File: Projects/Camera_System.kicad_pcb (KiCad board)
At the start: 2 copper layers, 10 parts, among them J1 BARREL_JACK, U1 IFX1117ME_V33, U2 LD2980ABM50TR

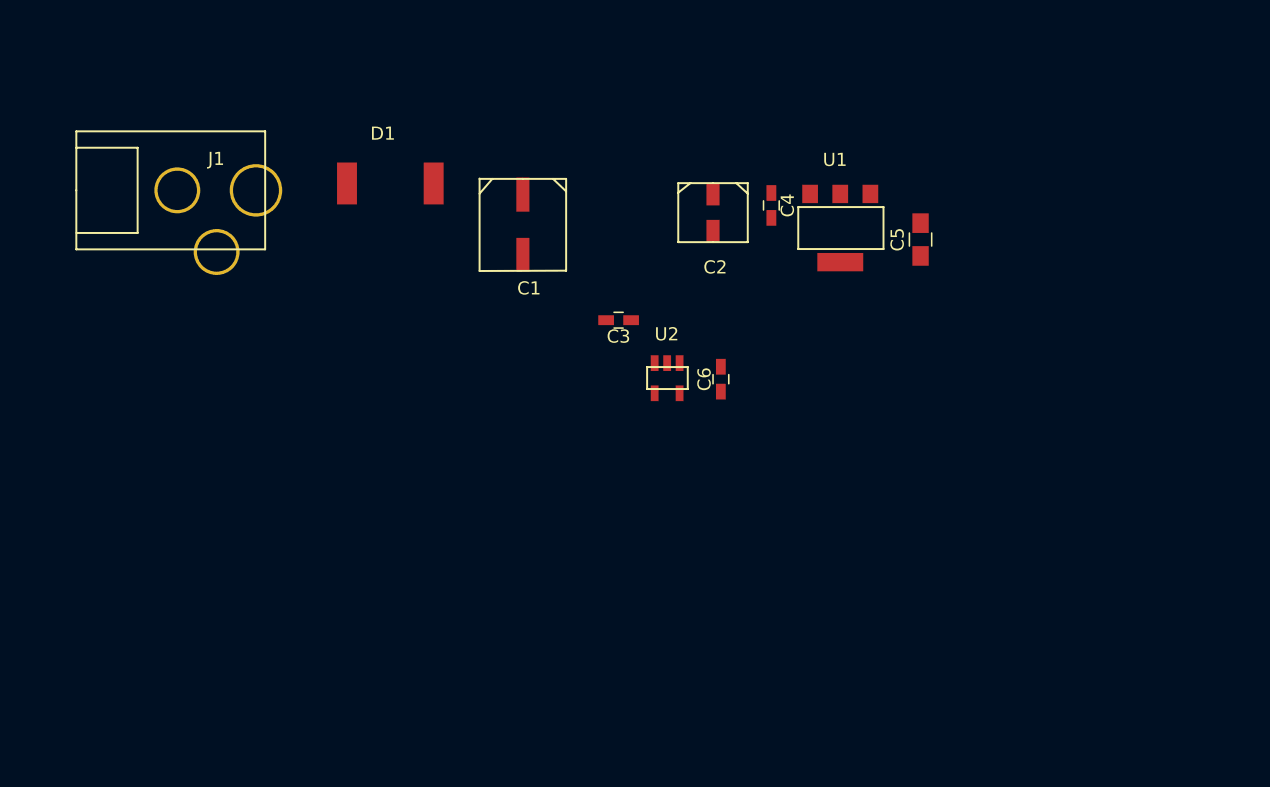
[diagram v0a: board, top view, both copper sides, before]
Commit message: New symbols habe been added
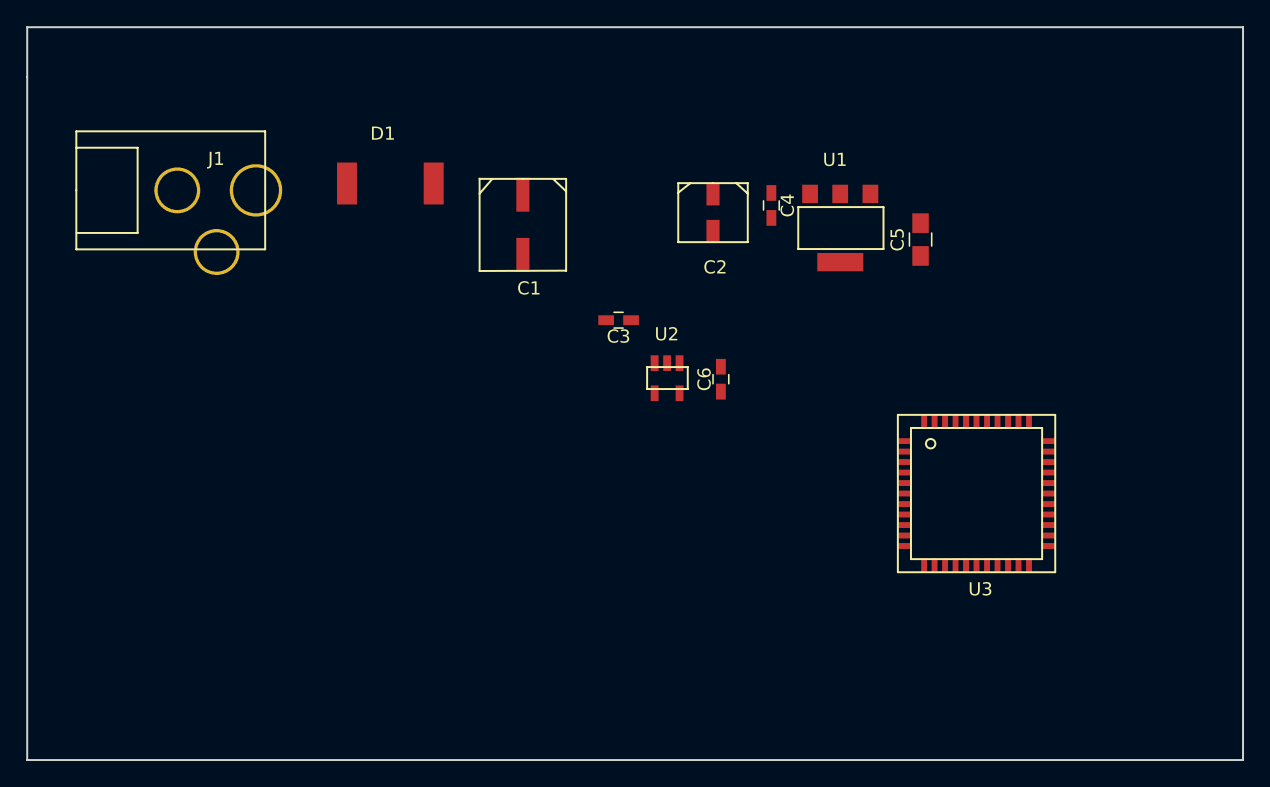
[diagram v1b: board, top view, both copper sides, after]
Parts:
- added U3: ATMEGA16A-AU, MyLibraries:ATMEGA16A-AU, F.Cu at (172.7, 121.9)
- C5: value 22u -> ???
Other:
- board outline added: 92.7 x 55.9 mm
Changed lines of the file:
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@@
 (kicad_pcb (version 4) (host pcbnew 4.0.6)
   (general
-    (links 20)
-    (no_connects 20)
+    (links 27)
+    (no_connects 27)
     (area 0 0 0 0)
     (thickness 1.6)
-    (drawings 0)
+    (drawings 5)
     (tracks 0)
     (zones 0)
-    (modules 10)
+    (modules 11)
     (nets 6)
   )
@@
       (effects (font (size 1 1) (thickness 0.15)))
     )
-    (fp_text value 22u (at 0 1.75 90) (layer F.Fab)
+    (fp_text value ??? (at 0 1.75 90) (layer F.Fab)
       (effects (font (size 1 1) (thickness 0.15)))
     )
@@
     (pad 4 smd rect (at 0.95 -2.3 180) (size 0.6 1.2) (layers F.Cu F.Paste F.Mask))
   )
+  (module MyLibraries:ATMEGA16A-AU (layer F.Cu)
+    (at 172.72 121.92)
+    (fp_text reference U3 (at 0.3 7.3) (layer F.SilkS)
+      (effects (font (size 1 1) (thickness 0.15)))
+    )
+    (fp_text value ATMEGA16A-AU (at 0.5 -7) (layer F.Fab)
+      (effects (font (size 1 1) (thickness 0.15)))
+    )
+    (fp_line (start -5 -5) (end 5 -5) (layer F.SilkS) (width 0.15))
+    (fp_line (start 5 -5) (end 5 5) (layer F.SilkS) (width 0.15))
+    (fp_line (start 5 5) (end -5 5) (layer F.SilkS) (width 0.15))
+    (fp_line (start -5 5) (end -5 -5) (layer F.SilkS) (width 0.15))
+    (fp_circle (center -3.5 -3.8) (end -3.2 -3.6) (layer F.SilkS) (width 0.15))
+    (fp_line (start -6 6) (end -6 -6) (layer F.SilkS) (width 0.15))
+    (fp_line (start -6 -6) (end 6 -6) (layer F.SilkS) (width 0.15))
+    (fp_line (start 6 -6) (end 6 6) (layer F.SilkS) (width 0.15))
+    (fp_line (start 6 6) (end -6 6) (layer F.SilkS) (width 0.15))
+    (pad 28 smd rect (at 5.5 0) (size 1.1 0.45) (layers F.Cu F.Paste F.Mask)
+      (net 1 GND))
+    (pad 29 smd rect (at 5.5 -0.8) (size 1.1 0.45) (layers F.Cu F.Paste F.Mask))
+    (pad 30 smd rect (at 5.5 -1.6) (size 1.1 0.45) (layers F.Cu F.Paste F.Mask))
+    (pad 31 smd rect (at 5.5 -2.4) (size 1.1 0.45) (layers F.Cu F.Paste F.Mask))
+    (pad 32 smd rect (at 5.5 -3.2) (size 1.1 0.45) (layers F.Cu F.Paste F.Mask))
+    (pad 33 smd rect (at 5.5 -4) (size 1.1 0.45) (layers F.Cu F.Paste F.Mask))
+    (pad 27 smd rect (at 5.5 0.8) (size 1.1 0.45) (layers F.Cu F.Paste F.Mask))
+    (pad 26 smd rect (at 5.5 1.6) (size 1.1 0.45) (layers F.Cu F.Paste F.Mask))
+    (pad 25 smd rect (at 5.5 2.4) (size 1.1 0.45) (layers F.Cu F.Paste F.Mask))
+    (pad 24 smd rect (at 5.5 3.2) (size 1.1 0.45) (layers F.Cu F.Paste F.Mask))
+    (pad 23 smd rect (at 5.5 4) (size 1.1 0.45) (layers F.Cu F.Paste F.Mask))
+    (pad 17 smd rect (at 0 5.5) (size 0.45 1.1) (layers F.Cu F.Paste F.Mask)
+      (net 2 +3V3))
+    (pad 18 smd rect (at 0.8 5.5) (size 0.45 1.1) (layers F.Cu F.Paste F.Mask)
+      (net 1 GND))
+    (pad 19 smd rect (at 1.6 5.5) (size 0.45 1.1) (layers F.Cu F.Paste F.Mask))
+    (pad 20 smd rect (at 2.4 5.5) (size 0.45 1.1) (layers F.Cu F.Paste F.Mask))
+    (pad 21 smd rect (at 3.2 5.5) (size 0.45 1.1) (layers F.Cu F.Paste F.Mask))
+    (pad 22 smd rect (at 4 5.5) (size 0.45 1.1) (layers F.Cu F.Paste F.Mask))
+    (pad 16 smd rect (at -0.8 5.5) (size 0.45 1.1) (layers F.Cu F.Paste F.Mask))
+    (pad 15 smd rect (at -1.6 5.5) (size 0.45 1.1) (layers F.Cu F.Paste F.Mask))
+    (pad 14 smd rect (at -2.4 5.5) (size 0.45 1.1) (layers F.Cu F.Paste F.Mask))
+    (pad 13 smd rect (at -3.2 5.5) (size 0.45 1.1) (layers F.Cu F.Paste F.Mask))
+    (pad 12 smd rect (at -4 5.5) (size 0.45 1.1) (layers F.Cu F.Paste F.Mask))
+    (pad 39 smd rect (at 0 -5.5) (size 0.45 1.1) (layers F.Cu F.Paste F.Mask)
+      (net 1 GND))
+    (pad 38 smd rect (at 0.8 -5.5) (size 0.45 1.1) (layers F.Cu F.Paste F.Mask)
+      (net 2 +3V3))
+    (pad 37 smd rect (at 1.6 -5.5) (size 0.45 1.1) (layers F.Cu F.Paste F.Mask))
+    (pad 36 smd rect (at 2.4 -5.5) (size 0.45 1.1) (layers F.Cu F.Paste F.Mask))
+    (pad 35 smd rect (at 3.2 -5.5) (size 0.45 1.1) (layers F.Cu F.Paste F.Mask))
+    (pad 34 smd rect (at 4 -5.5) (size 0.45 1.1) (layers F.Cu F.Paste F.Mask))
+    (pad 40 smd rect (at -0.8 -5.5) (size 0.45 1.1) (layers F.Cu F.Paste F.Mask))
+    (pad 41 smd rect (at -1.6 -5.5) (size 0.45 1.1) (layers F.Cu F.Paste F.Mask))
+    (pad 42 smd rect (at -2.4 -5.5) (size 0.45 1.1) (layers F.Cu F.Paste F.Mask))
+    (pad 43 smd rect (at -3.2 -5.5) (size 0.45 1.1) (layers F.Cu F.Paste F.Mask))
+    (pad 44 smd rect (at -4 -5.5) (size 0.45 1.1) (layers F.Cu F.Paste F.Mask))
+    (pad 6 smd rect (at -5.5 0) (size 1.1 0.45) (layers F.Cu F.Paste F.Mask)
+      (net 1 GND))
+    (pad 5 smd rect (at -5.5 -0.8) (size 1.1 0.45) (layers F.Cu F.Paste F.Mask)
+      (net 2 +3V3))
+    (pad 4 smd rect (at -5.5 -1.6) (size 1.1 0.45) (layers F.Cu F.Paste F.Mask))
+    (pad 3 smd rect (at -5.5 -2.4) (size 1.1 0.45) (layers F.Cu F.Paste F.Mask))
+    (pad 2 smd rect (at -5.5 -3.2) (size 1.1 0.45) (layers F.Cu F.Paste F.Mask))
+    (pad 1 smd rect (at -5.5 -4) (size 1.1 0.45) (layers F.Cu F.Paste F.Mask))
+    (pad 7 smd rect (at -5.5 0.8) (size 1.1 0.45) (layers F.Cu F.Paste F.Mask))
+    (pad 8 smd rect (at -5.5 1.6) (size 1.1 0.45) (layers F.Cu F.Paste F.Mask))
+    (pad 9 smd rect (at -5.5 2.4) (size 1.1 0.45) (layers F.Cu F.Paste F.Mask))
+    (pad 10 smd rect (at -5.5 3.2) (size 1.1 0.45) (layers F.Cu F.Paste F.Mask))
+    (pad 11 smd rect (at -5.5 4) (size 1.1 0.45) (layers F.Cu F.Paste F.Mask))
+  )
+  (gr_line (start 100.33 86.36) (end 100.33 90.17) (angle 90) (layer Edge.Cuts) (width 0.15))
+  (gr_line (start 193.04 86.36) (end 100.33 86.36) (angle 90) (layer Edge.Cuts) (width 0.15))
+  (gr_line (start 193.04 142.24) (end 193.04 86.36) (angle 90) (layer Edge.Cuts) (width 0.15))
+  (gr_line (start 100.33 142.24) (end 193.04 142.24) (angle 90) (layer Edge.Cuts) (width 0.15))
+  (gr_line (start 100.33 90.17) (end 100.33 142.24) (angle 90) (layer Edge.Cuts) (width 0.15))
 )

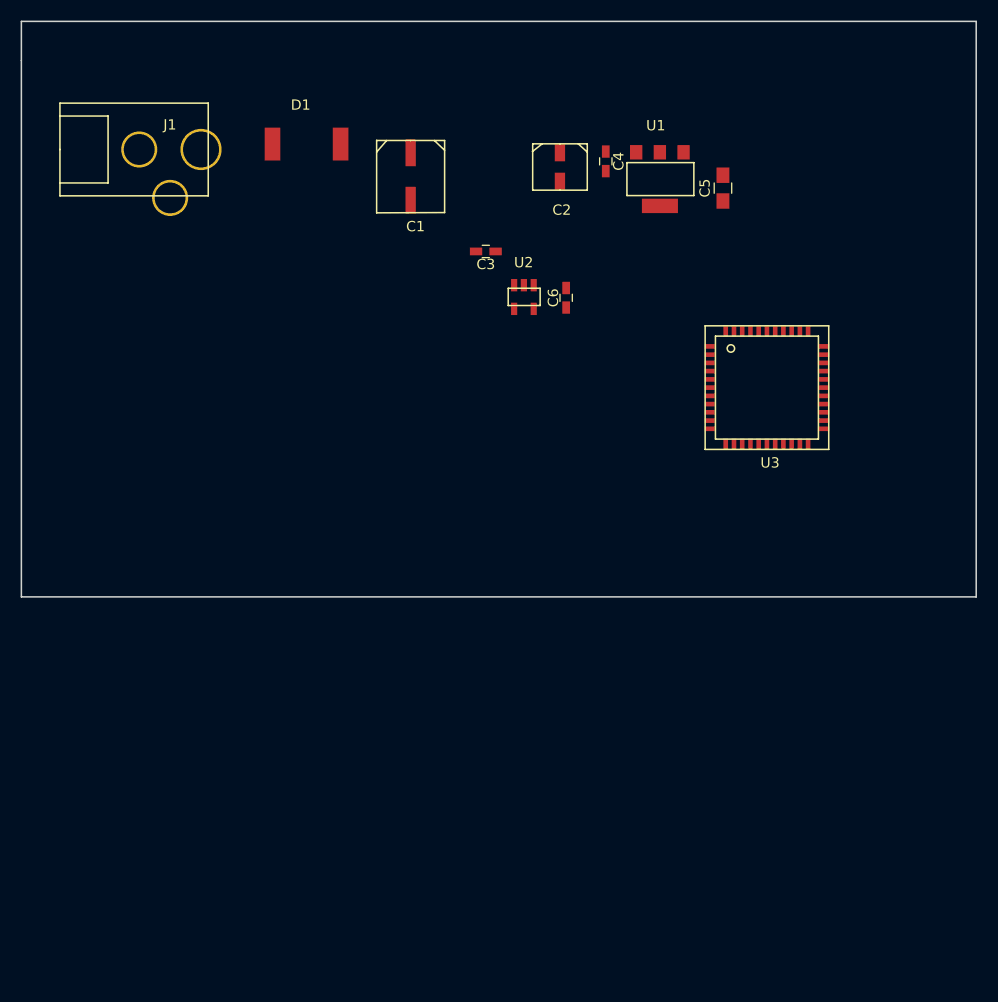
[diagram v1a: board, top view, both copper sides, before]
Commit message: New footprints have been created
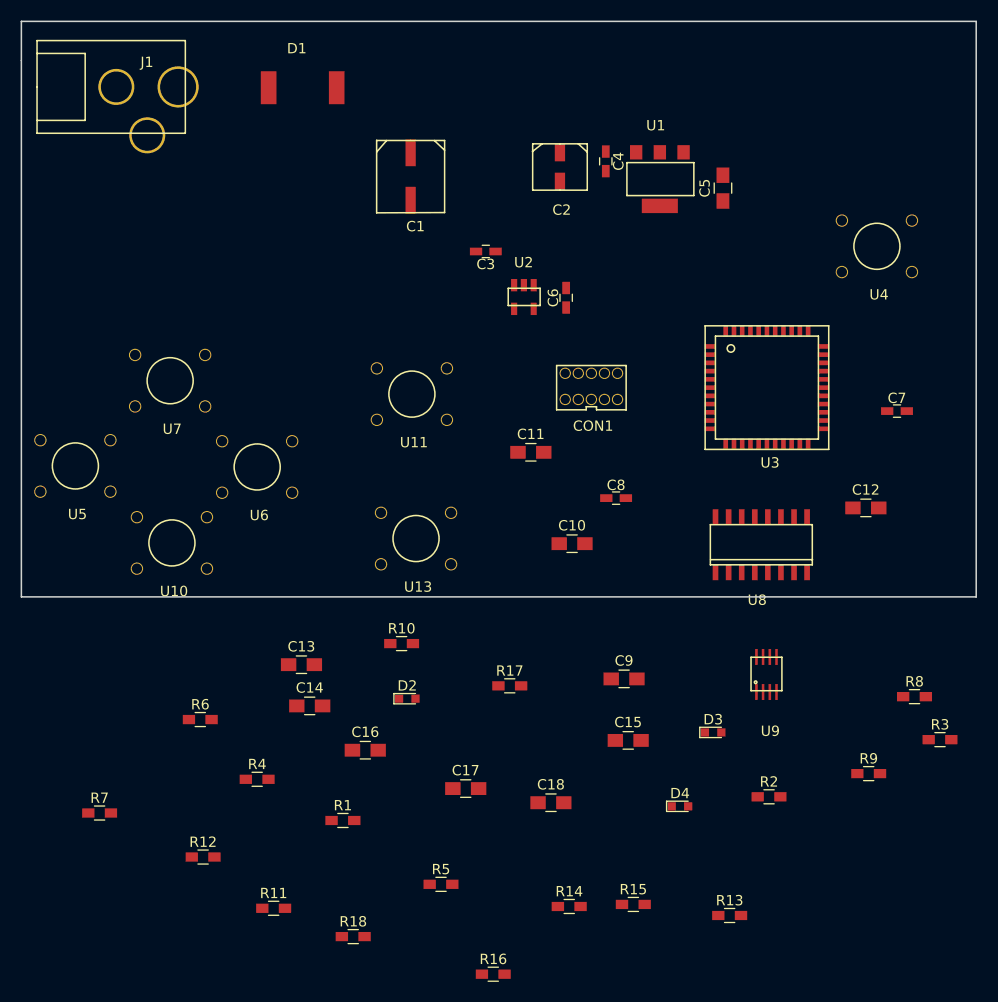
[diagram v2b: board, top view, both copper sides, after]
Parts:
- added C10: 100n, Capacitors_SMD:C_0805_HandSoldering, F.Cu at (153.8, 137.1)
- added C11: 100n, Capacitors_SMD:C_0805_HandSoldering, F.Cu at (149.8, 128.2)
- added C12: 100n, Capacitors_SMD:C_0805_HandSoldering, F.Cu at (182.3, 133.6)
- added C13: 100n, Capacitors_SMD:C_0805_HandSoldering, F.Cu at (127.5, 148.8)
- added C14: 100n, Capacitors_SMD:C_0805_HandSoldering, F.Cu at (128.3, 152.8)
- added C15: 100n, Capacitors_SMD:C_0805_HandSoldering, F.Cu at (159.2, 156.2)
- added C16: 100n, Capacitors_SMD:C_0805_HandSoldering, F.Cu at (133.7, 157.1)
- added C17: 100n, Capacitors_SMD:C_0805_HandSoldering, F.Cu at (143.5, 160.8)
- added C18: 100n, Capacitors_SMD:C_0805_HandSoldering, F.Cu at (151.8, 162.2)
- added C7: 12p, Capacitors_SMD:C_0603_HandSoldering, F.Cu at (185.3, 124.2)
- added C8: 12p, Capacitors_SMD:C_0603_HandSoldering, F.Cu at (158.1, 132.7)
- added C9: 100n, Capacitors_SMD:C_0805_HandSoldering, F.Cu at (158.8, 150.2)
- added CON1: AVR-ISP-10, MyLibraries:N2510-6002RB, F.Cu at (155.7, 121.8)
- added D2: LED, LEDs:LED_0603, F.Cu at (137.8, 152.1)
- added D3: LED, LEDs:LED_0603, F.Cu at (167.5, 155.4)
- added D4: LED, LEDs:LED_0603, F.Cu at (164.3, 162.6)
- added R1: 0, Resistors_SMD:R_0603_HandSoldering, F.Cu at (131.6, 163.9)
- added R10: 1.74k, Resistors_SMD:R_0603_HandSoldering, F.Cu at (137.2, 146.8)
- added R11: 10k, Resistors_SMD:R_0603_HandSoldering, F.Cu at (124.8, 172.5)
- added R12: 10k, Resistors_SMD:R_0603_HandSoldering, F.Cu at (118.0, 167.5)
- added R13: 200k, Resistors_SMD:R_0603_HandSoldering, F.Cu at (169.1, 173.2)
- added R14: 10k, Resistors_SMD:R_0603_HandSoldering, F.Cu at (153.5, 172.3)
- added R15: 10k, Resistors_SMD:R_0603_HandSoldering, F.Cu at (159.8, 172.1)
- added R16: 4.7k, Resistors_SMD:R_0603_HandSoldering, F.Cu at (146.2, 178.9)
- added R17: 24.9, Resistors_SMD:R_0603_HandSoldering, F.Cu at (147.8, 150.9)
- added R18: 4.7k, Resistors_SMD:R_0603_HandSoldering, F.Cu at (132.6, 175.2)
- added R2: 620, Resistors_SMD:R_0603_HandSoldering, F.Cu at (172.9, 161.7)
- added R3: 10k, Resistors_SMD:R_0603_HandSoldering, F.Cu at (189.5, 156.1)
- added R4: 620, Resistors_SMD:R_0603_HandSoldering, F.Cu at (123.2, 159.9)
- added R5: 1k, Resistors_SMD:R_0603_HandSoldering, F.Cu at (141.1, 170.2)
- added R6: 10k, Resistors_SMD:R_0603_HandSoldering, F.Cu at (117.7, 154.2)
- added R7: 10k, Resistors_SMD:R_0603_HandSoldering, F.Cu at (107.9, 163.2)
- added R8: 10k, Resistors_SMD:R_0603_HandSoldering, F.Cu at (187.1, 151.9)
- added R9: 1.74k, Resistors_SMD:R_0603_HandSoldering, F.Cu at (182.6, 159.4)
- added U10: RT1105AF160Q, MyLibraries:RT1105AF160Q, F.Cu at (115.0, 137.0)
- added U11: RT1105AF160Q, MyLibraries:RT1105AF160Q, F.Cu at (138.2, 122.5)
- added U13: RT1105AF160Q, MyLibraries:RT1105AF160Q, F.Cu at (138.7, 136.6)
- added U4: RT1105AF160Q, MyLibraries:RT1105AF160Q, F.Cu at (183.4, 108.2)
- added U5: RT1105AF160Q, MyLibraries:RT1105AF160Q, F.Cu at (105.6, 129.5)
- added U6: RT1105AF160Q, MyLibraries:RT1105AF160Q, F.Cu at (123.2, 129.6)
- added U7: RT1105AF160Q, MyLibraries:RT1105AF160Q, F.Cu at (114.8, 121.2)
- added U8: CD4014B, MyLibraries:CD4014B_SOIC, F.Cu at (172.2, 137.2)
- added U9: PCA9306, MyLibraries:PCA9306_SM8, F.Cu at (172.7, 149.8)
- C5: value ??? -> 22u
- moved J1 6.47 mm to (112.5, 92.7)
- moved D1 5.49 mm to (130.9, 92.8)
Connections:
- U3 pad 1: (no net) -> /MOSI
- U3 pad 14: (no net) -> /P_S_CLK
- U3 pad 19: (no net) -> /3V3_SCL
- U3 pad 2: (no net) -> /MISO
- U3 pad 20: (no net) -> /3V3_SDA
- U3 pad 27: (no net) -> +3V3
- U3 pad 29: (no net) -> Net-(C9-Pad1)
- U3 pad 3: (no net) -> /SCK
- U3 pad 4: (no net) -> /MIC_RST
- U3 pad 40: (no net) -> /SERIAL_IN
- U3 pad 41: (no net) -> /P_S_CTRL
- U3 pad 43: (no net) -> Net-(R1-Pad2)
- U3 pad 7: (no net) -> Net-(C7-Pad1)
- U3 pad 8: (no net) -> Net-(C8-Pad1)

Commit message: Schematic has been finished and layout started
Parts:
- added U12: LCD_1602, MyLibraries:LCD_header_2.5_4, F.Cu at (158.9, 43.6)
- added U14: Si501, MyLibraries:Si501_2x2.5, F.Cu at (233.6, 152.7)
- added U15: OV7670-nofifo, MyLibraries:Camera_ov7670_2.5_2x9, F.Cu at (106.6, 152.7)
- added U16: ESP8266, MyLibraries:wifi_header_female_2.5_2x4, F.Cu at (91.9, 79.8)
- added U17: SDCARD, MyLibraries:SDCARD_2.5_6, F.Cu at (70.2, 98.3)
- added Y1: Crystal, MyLibraries:LFXTAL003210, F.Cu at (93.0, 108.3)
- C7, C8: value 12p -> 22p
- moved R5 129.0 mm to (146.7, 41.2), turned to 90 degrees
- moved R13 128.4 mm to (149.6, 46.3), turned to 270 degrees
- moved D4 125.7 mm to (145.8, 38.2)
- moved R9 119.2 mm to (155.1, 43.5), turned to 270 degrees
- moved D3 112.4 mm to (120.0, 53.6), turned to 270 degrees
- moved R12 110.4 mm to (221.4, 129.0)
- moved C14 104.8 mm to (148.3, 50.0), turned to 180 degrees
- moved R10 104.4 mm to (152.5, 43.5), turned to 270 degrees
- moved R2 103.0 mm to (96.7, 92.5), turned to 90 degrees
- moved R7 102.9 mm to (205.0, 129.0)
- moved R4 102.1 mm to (120.0, 58.0), turned to 90 degrees
- moved C7 99.7 mm to (87.6, 104.5), turned to 270 degrees
- moved U9 99.0 mm to (146.9, 54.1), turned to 270 degrees
- moved C12 98.1 mm to (149.6, 41.1), turned to 90 degrees
- moved C13 96.5 mm to (216.1, 110.6), turned to 180 degrees
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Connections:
- R15 pad 1: (no net) -> Net-(R15-Pad1)
- R17 pad 2: (no net) -> Net-(R17-Pad2)
- U3 pad 10: (no net) -> /WLAN_TX
- U3 pad 11: (no net) -> /CAM_RST
- U3 pad 12: (no net) -> /CAM_PWDN
- U3 pad 13: (no net) -> /CAM_D1
- U3 pad 15: (no net) -> /CAM_HREF
- U3 pad 16: (no net) -> /CAM_VSINC
- U3 pad 21: (no net) -> /WLAN_CHPD
- U3 pad 22: (no net) -> /WLAN_RST
- U3 pad 23: (no net) -> /WLAN_GPIO0
- U3 pad 24: (no net) -> /WLAN_GPIO2
- U3 pad 30: (no net) -> /CAM_D7
- U3 pad 31: (no net) -> /CAM_D6
- U3 pad 32: (no net) -> /CAM_D5
- U3 pad 33: (no net) -> /CAM_D4
- U3 pad 34: (no net) -> /CAM_D3
- U3 pad 35: (no net) -> /CAM_D2
- U3 pad 36: (no net) -> /CAM_PCLK
- U3 pad 37: (no net) -> /CAM_D0
- U3 pad 44: (no net) -> /SDC_CS
- U3 pad 9: (no net) -> /WLAN_RX
- U8 pad 13: /CTRL_BTN2 -> /CTRL_BTN1
- U8 pad 4: /CTRL_BTN1 -> /CTRL_UP
- U8 pad 6: /CTRL_UP -> /CTRL_RIGHT
- U8 pad 7: /CTRL_RIGHT -> /CTRL_BTN2
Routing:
- net +3V3: track 0.00 -> 106.2 mm, vias 0 -> 3
- net /CTRL_BTN2: track 0.00 -> 36.5 mm, vias 0 -> 2
- net /CTRL_LEFT: track 0.00 -> 36.5 mm
- net /VDC_IN: track 0.00 -> 33.2 mm
- net /CTRL_DOWN: track 0.00 -> 32.3 mm, vias 0 -> 1
- net /5V_SDA: track 0.00 -> 23.3 mm
- net /CTRL_RIGHT: track 0.00 -> 21.3 mm
- net +5V: track 0.00 -> 19.9 mm
- net /5V_SCL: track 0.00 -> 19.4 mm
- net /MISO: track 0.00 -> 18.4 mm
- net /CTRL_BTN1: track 0.00 -> 18.1 mm
- net Net-(C8-Pad1): track 0.00 -> 17.9 mm
- net /CTRL_UP: track 0.00 -> 17.3 mm
- net /SCK: track 0.00 -> 17.2 mm
- net Net-(C7-Pad1): track 0.00 -> 17.1 mm
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- added copper zone on B.Cu, net GND
- added copper zone on F.Cu, net GND
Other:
- board size 92.7 x 55.9 mm -> 219.3 x 160.9 mm
- net class Power added: clearance 0.2, trace_width 1, via_dia 0.6, via_drill 0.4
